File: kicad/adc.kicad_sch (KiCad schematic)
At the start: 14 parts, among them U1 AD7606C-16BSTZ

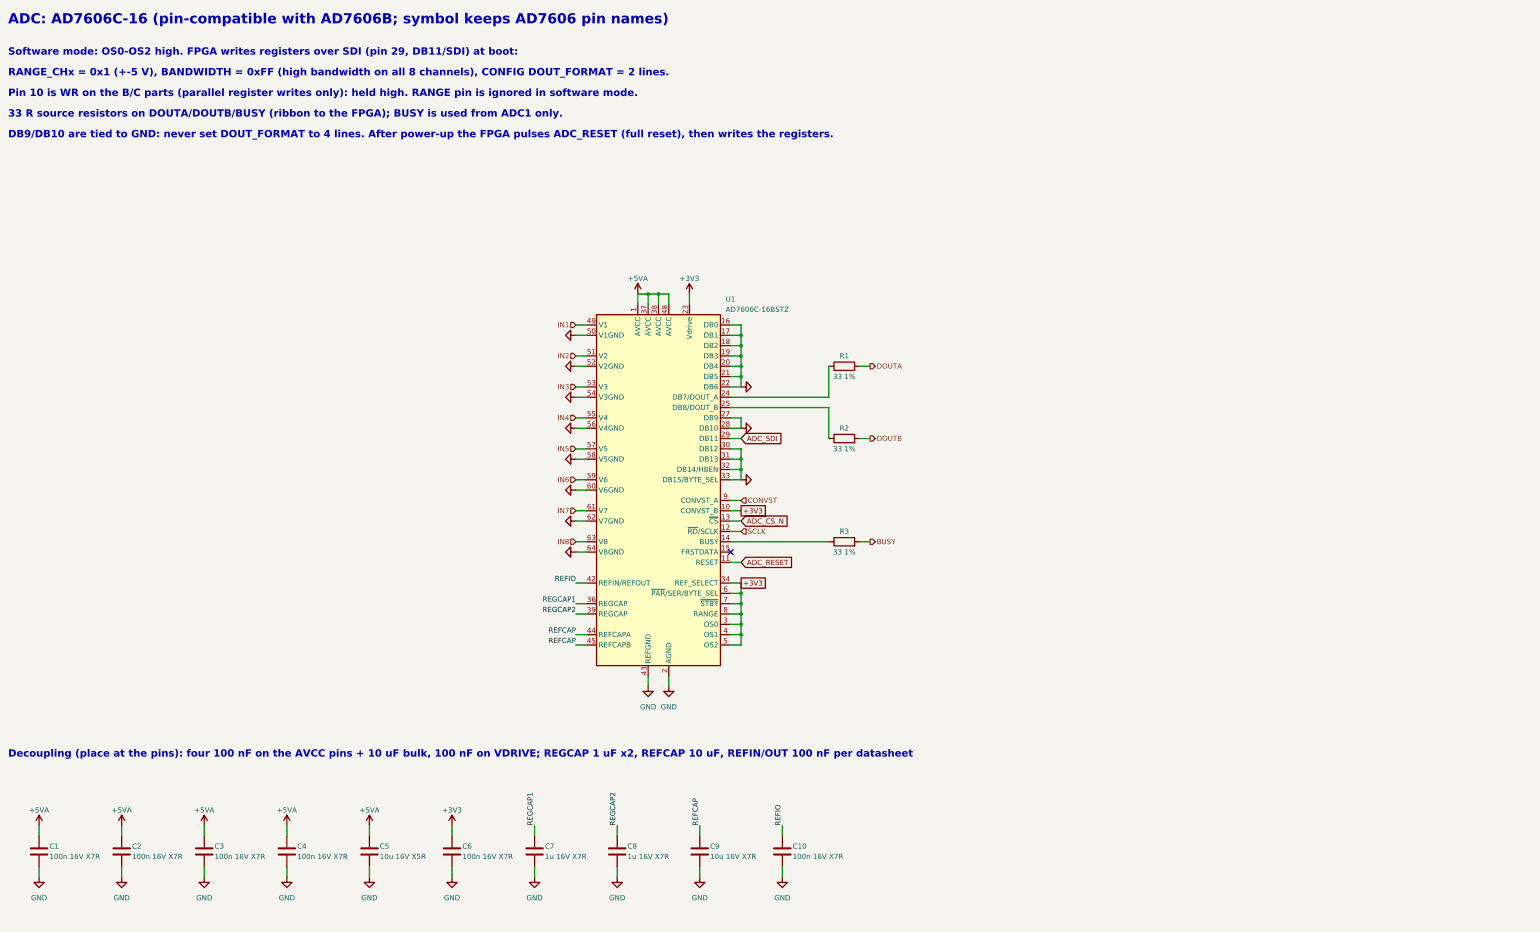
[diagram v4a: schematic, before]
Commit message: Switch to 16 x TLV320ADC5140, +3V3A rail, 3 A buck, datasheet library, transducer DNP
- ADC: 8 x AD7606C-16 ($470/board) -> 16 x TI TLV320ADC5140 at 192 kSPS ($50/board): TDM slave on a
  shared BCLK/FSYNC, I2C (SCL + 4 SDA groups), 2k/1k + 100 nF input network; project symbol from
  scripts/make_symbols.py; 9 clock buffers; J2 remapped
- power: +3V3A (second TPS7A4700, ANY-OUT 3.3 V); +5V buck TPS54202 -> TPS54302 (3 A), L1 10 uH 5 A
- checks and simulations updated for the new ADC input (all 18 checks and 10 sims pass)
- docs/datasheets: a PDF for every part, kept in step by scripts/datasheets.py (run by bom.py)
- design brief section 5a: interface bandwidth budget (no bus is a bottleneck; TX_EDGE = 1)
- CUSA-TR65 marked DNP for JLCPCB (hand-soldered), priced at DigiKey 100+
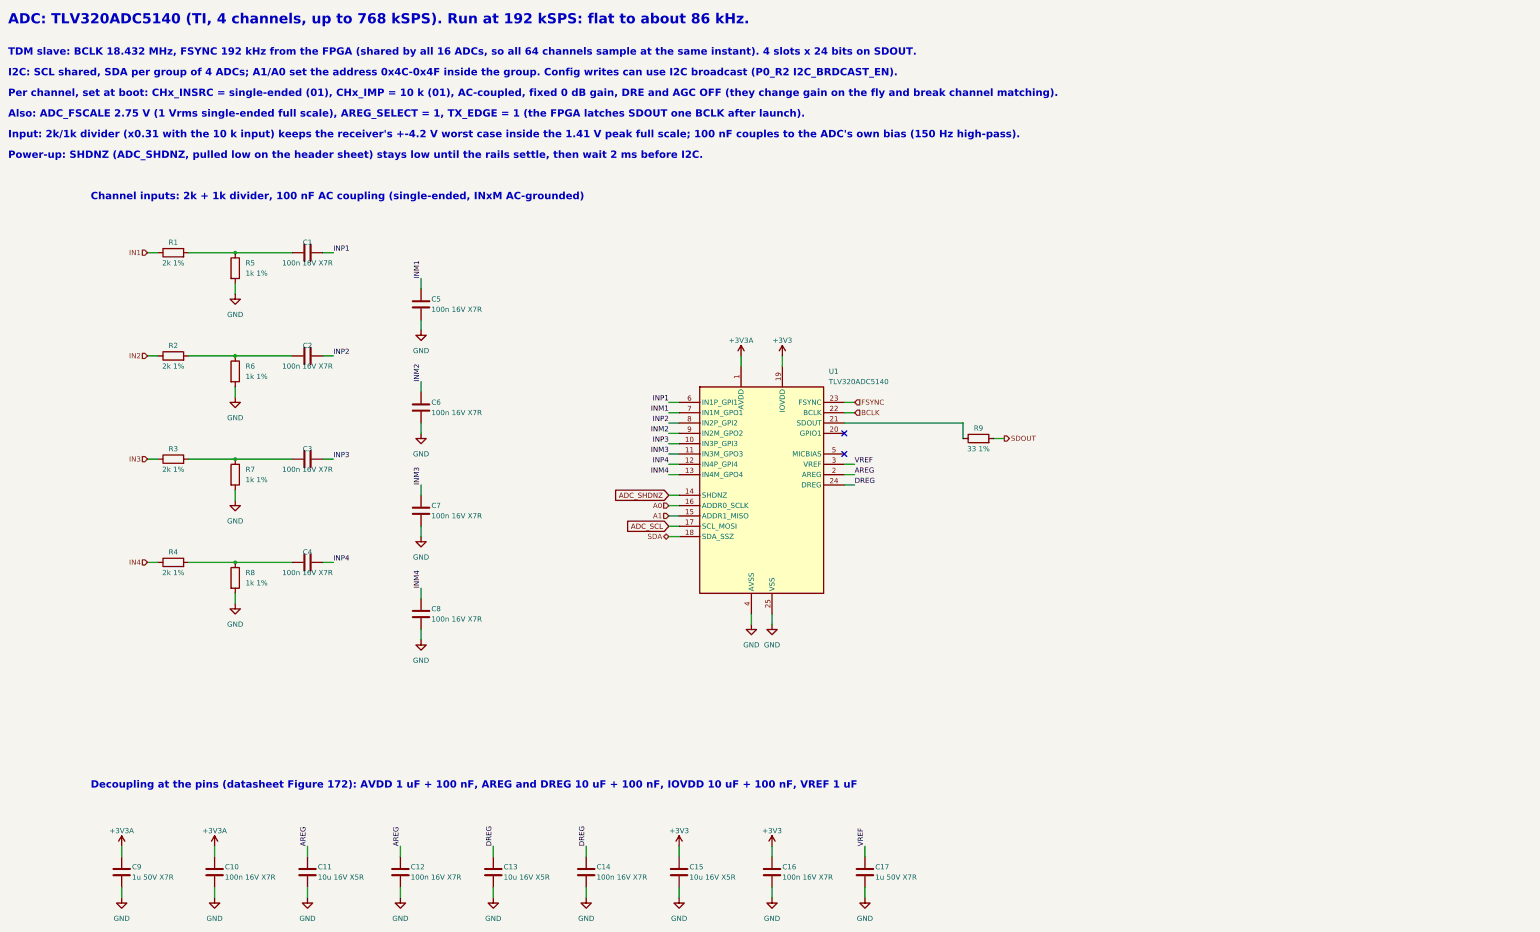
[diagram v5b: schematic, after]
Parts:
- removed U1: AD7606C-16BSTZ, Package_QFP:LQFP-64_10x10mm_P0.5mm, symbol Analog_ADC:AD7606
- added C11, C13, C15: 10u 16V X5R, Capacitor_SMD:C_0805_2012Metric, symbol Device:C
- added C12, C14, C16: 100n 16V X7R, Capacitor_SMD:C_0603_1608Metric, symbol Device:C
- added C17: 1u 50V X7R, Capacitor_SMD:C_0805_2012Metric, symbol Device:C
- added R4: 2k 1%, Resistor_SMD:R_0603_1608Metric, symbol Device:R
- added R5, R6, R7, R8: 1k 1%, Resistor_SMD:R_0603_1608Metric, symbol Device:R
- added R9: 33 1%, Resistor_SMD:R_0603_1608Metric, symbol Device:R
- added U1: TLV320ADC5140, Package_DFN_QFN:Texas_RTW_WQFN-24-1EP_4x4mm_P0.5mm_EP2.7x2.7mm_ThermalVias, symbol aesa:TLV320ADC5140
- C5: value 10u 16V X5R -> 100n 16V X7R; footprint Capacitor_SMD:C_0805_2012Metric -> Capacitor_SMD:C_0603_1608Metric; LCSC C15850 -> C14663
- C7, C8: value 1u 16V X7R -> 100n 16V X7R; LCSC C388002 -> C14663
- C9: value 10u 16V X7R -> 1u 50V X7R; footprint Capacitor_SMD:C_1206_3216Metric -> Capacitor_SMD:C_0805_2012Metric; LCSC C380363 -> C28323
- R1, R2, R3: value 33 1% -> 2k 1%; LCSC C23140 -> C22975
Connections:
- net REFIO is gone; now on net +3V3A: C10.1
- net +3V3: now also C15.1, C16.1, U1.19 (IOVDD); no longer C6.1
- net GND: now also C11.2, C12.2, C13.2, C14.2, C15.2, C16.2, C17.2, R5.2, R6.2, R7.2, R8.2, U1.25 (VSS), U1.4 (AVSS); no longer C1.2, C2.2, C3.2, C4.2
- net IN1: now also R1.1
- net IN2: now also R2.1
- net IN3: now also R3.1
- net IN4: now also R4.1
- removed net +5VA: C1.1, C2.1, C3.1, C4.1, C5.1
- net BUSY: no longer names the net of R3.2
- net BUSY: now also C3.1, R7.1
- net DOUTA: no longer names the net of R1.2
- net DOUTA: now also C1.1, R5.1
- net DOUTB: no longer names the net of R2.2
- net DOUTB: now also C2.1, R6.1
- net REFCAP renamed +3V3A
- net +3V3A: now also U1.1 (AVDD)
- net REGCAP1 renamed INM3
- net INM3: now also U1.11 (IN3M_GPO3)
- net REGCAP2 renamed INM4
- net INM4: now also U1.13 (IN4M_GPO4)
- new net: C4.1, R4.2, R8.1
- new net: R9.1, U1.21 (SDOUT)
- new net A0: U1.16 (ADDR0_SCLK)
- new net A1: U1.15 (ADDR1_MISO)
- new net ADC_SCL: U1.17 (SCL_MOSI)
- new net ADC_SHDNZ: U1.14 (SHDNZ)
- new net AREG: C11.1, C12.1, U1.2 (AREG)
- new net BCLK: U1.22 (BCLK)
- new net DREG: C13.1, C14.1, U1.24 (DREG)
- new net FSYNC: U1.23 (FSYNC)
- new net INM1: C5.1, U1.7 (IN1M_GPO1)
- new net INM2: C6.1, U1.9 (IN2M_GPO2)
- new net INP1: C1.2, U1.6 (IN1P_GPI1)
- new net INP2: C2.2, U1.8 (IN2P_GPI2)
- new net INP3: C3.2, U1.10 (IN3P_GPI3)
- new net INP4: C4.2, U1.12 (IN4P_GPI4)
- new net SDA: U1.18 (SDA_SSZ)
- new net SDOUT: R9.2
- new net VREF: C17.1, U1.3 (VREF)
- no-connect marks 1 -> 2
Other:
- note added: "ADC: TLV320ADC5140 (TI, 4 channels, up to 768 kSPS). Run at 192 kSPS: flat to about 86 kHz."
- note added: "Also: ADC_FSCALE 2.75 V (1 Vrms single-ended full scale), AREG_SELECT = 1, TX_EDGE = 1 (the FPGA latches SDOUT one BCLK after launch)."
- note added: "Channel inputs: 2k + 1k divider, 100 nF AC coupling (single-ended, INxM AC-grounded)"
- note added: "Decoupling at the pins (datasheet Figure 172): AVDD 1 uF + 100 nF, AREG and DREG 10 uF + 100 nF, IOVDD 10 uF + 100 nF, VREF 1 uF"
- note added: "I2C: SCL shared, SDA per group of 4 ADCs; A1/A0 set the address 0x4C-0x4F inside the group. Config writes can use I2C broadcast (P0_R2 I2C_BRDCAST_EN)."
- note added: "Input: 2k/1k divider (x0.31 with the 10 k input) keeps the receiver's +-4.2 V worst case inside the 1.41 V peak full scale; 100 nF couples to the ADC's own bias (150 Hz high-pass)."
- note added: "Per channel, set at boot: CHx_INSRC = single-ended (01), CHx_IMP = 10 k (01), AC-coupled, fixed 0 dB gain, DRE and AGC OFF (they change gain on the fly and break channel matching)."
- note added: "Power-up: SHDNZ (ADC_SHDNZ, pulled low on the header sheet) stays low until the rails settle, then wait 2 ms before I2C."
- note added: "TDM slave: BCLK 18.432 MHz, FSYNC 192 kHz from the FPGA (shared by all 16 ADCs, so all 64 channels sample at the same instant). 4 slots x 24 bits on SDOUT."
- note removed: "33 R source resistors on DOUTA/DOUTB/BUSY (ribbon to the FPGA); BUSY is used from ADC1 only."
- note removed: "ADC: AD7606C-16 (pin-compatible with AD7606B; symbol keeps AD7606 pin names)"
- note removed: "DB9/DB10 are tied to GND: never set DOUT_FORMAT to 4 lines. After power-up the FPGA pulses ADC_RESET (full reset), then writes the registers."
- note removed: "Decoupling (place at the pins): four 100 nF on the AVCC pins + 10 uF bulk, 100 nF on VDRIVE; REGCAP 1 uF x2, REFCAP 10 uF, REFIN/OUT 100 nF per datasheet"
- note removed: "Pin 10 is WR on the B/C parts (parallel register writes only): held high. RANGE pin is ignored in software mode."
- note removed: "RANGE_CHx = 0x1 (+-5 V), BANDWIDTH = 0xFF (high bandwidth on all 8 channels), CONFIG DOUT_FORMAT = 2 lines."
- note removed: "Software mode: OS0-OS2 high. FPGA writes registers over SDI (pin 29, DB11/SDI) at boot:"
- title: ADC (x8): AD7606C-16, software mode, serial 2 DOUT -> ADC (x16): TLV320ADC5140, 4 channels, 192 kSPS TDM

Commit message: Block-first routing: all repeated blocks routed and passing, power input and +-6V5 hand-routed
Schematic
- TX groups and ADC inputs numbered in order (TXG01 = DRV1-4, ADC IN1..4 = RX1..4).
- Power sheets renumbered 1-8 with real references; eFuse RTN no longer tied to GND (TPS2660 9.3.5.5).
- Damped 100 uF bulk caps at the far ends of VIN (C50) and +5V (C51); header clock RC filters removed;
  switch-node snubbers kept as DNP footprints.

Layout and routing
- New routing toolchain: route.py (block stages), block_routes.py (hand-made block routes), maze.py
  (45-degree grid router with rip-up and a per-net time budget), route_lib.py (bend45, chamfer, copper
  checks), block_check.py (DRC and internal nets per block instance), board/cell views.
- Channel, ADC, TX group, clock buffer, enable buffer, mic and header blocks routed and passing
  block_check; no right-angle corners left.
- Designed TX control bus; SDI taps keep 0.7 mm from clock copper.
- Power: 12 V input (eFuse, RTN island, FLT via the front copper) and TPS65131 +-6V5 section with fixed
  templates and hand routing; each power section counts as its own block; the +3V3 LED overflows into
  the gap beside its section.

docs/routing_and_emi.md describes the routing and EMI rules; sim/mic_clock_si adds the mic clock check.
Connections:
- net IN1: now also R4.1; no longer R1.1
- net IN2: now also R3.1; no longer R2.1
- net IN3: now also R2.1; no longer R3.1
- net IN4: now also R1.1; no longer R4.1
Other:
- note added: "Ports IN1-IN4 are the block's four elements in order; IN1 feeds ADC channel 4 ... IN4 channel 1 (the order the receive lanes reach the inputs on the board). TDM: channel c carries element 4k-4 + (5 - c)."
